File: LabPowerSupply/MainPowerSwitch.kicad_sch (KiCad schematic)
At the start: 3 parts

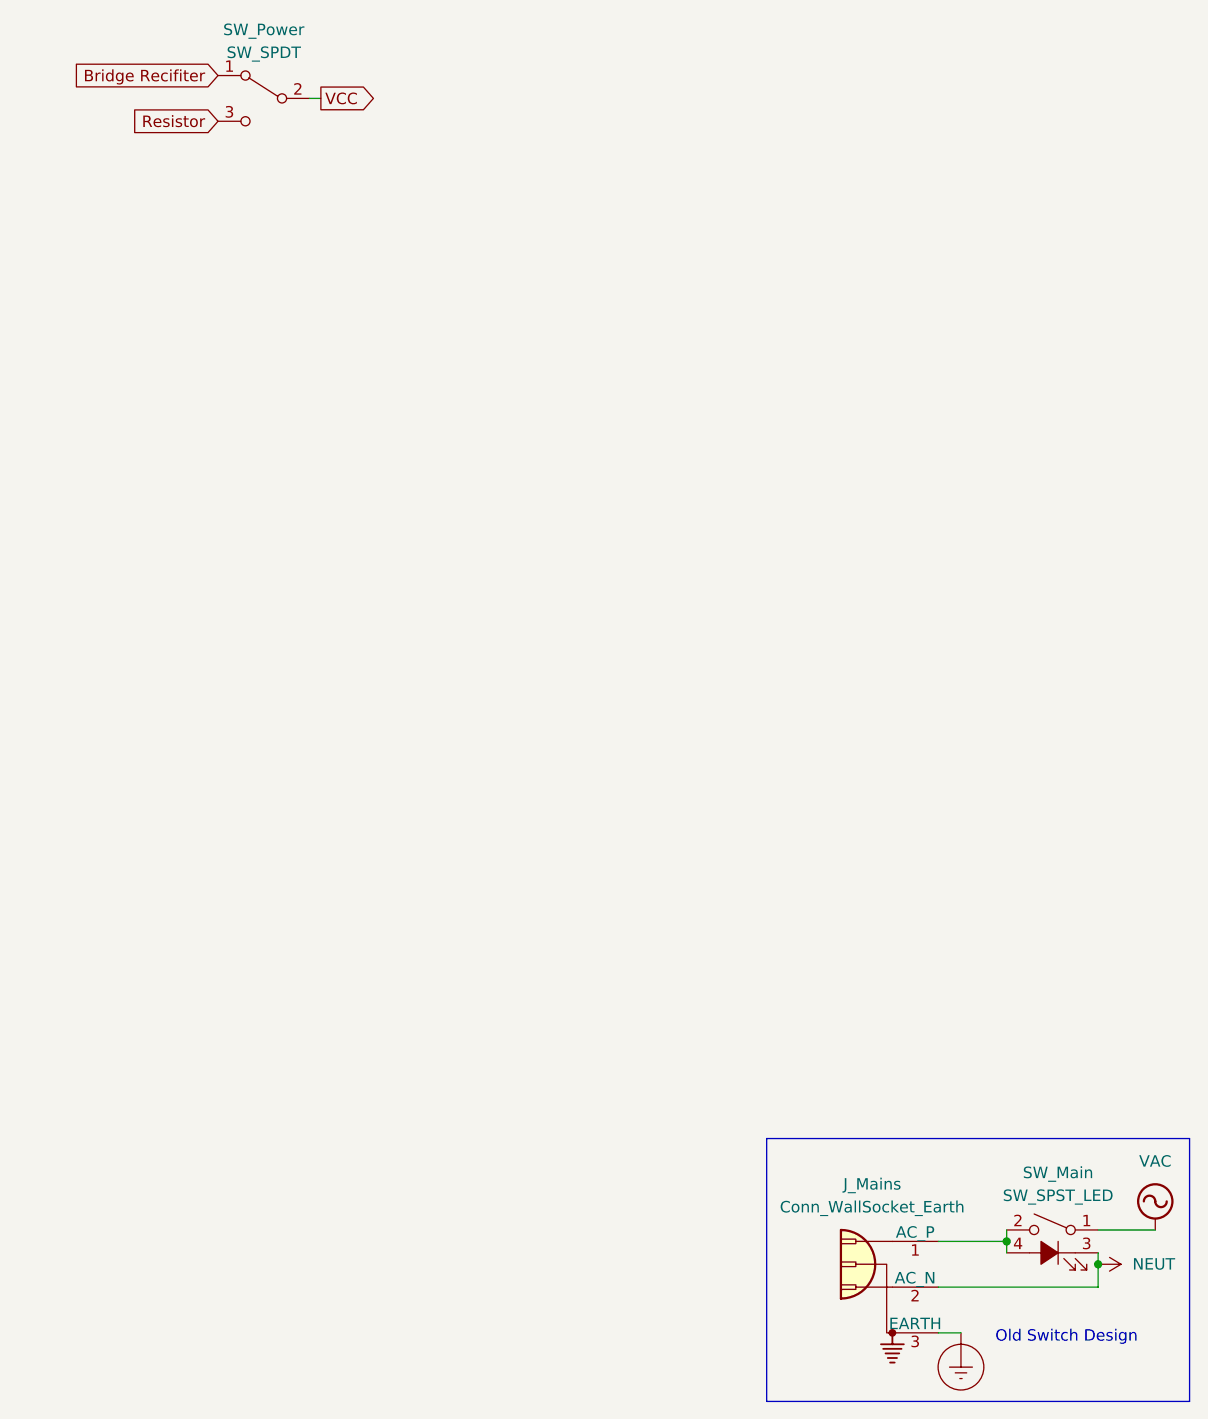
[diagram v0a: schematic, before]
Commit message: Finished first pass on the schematic
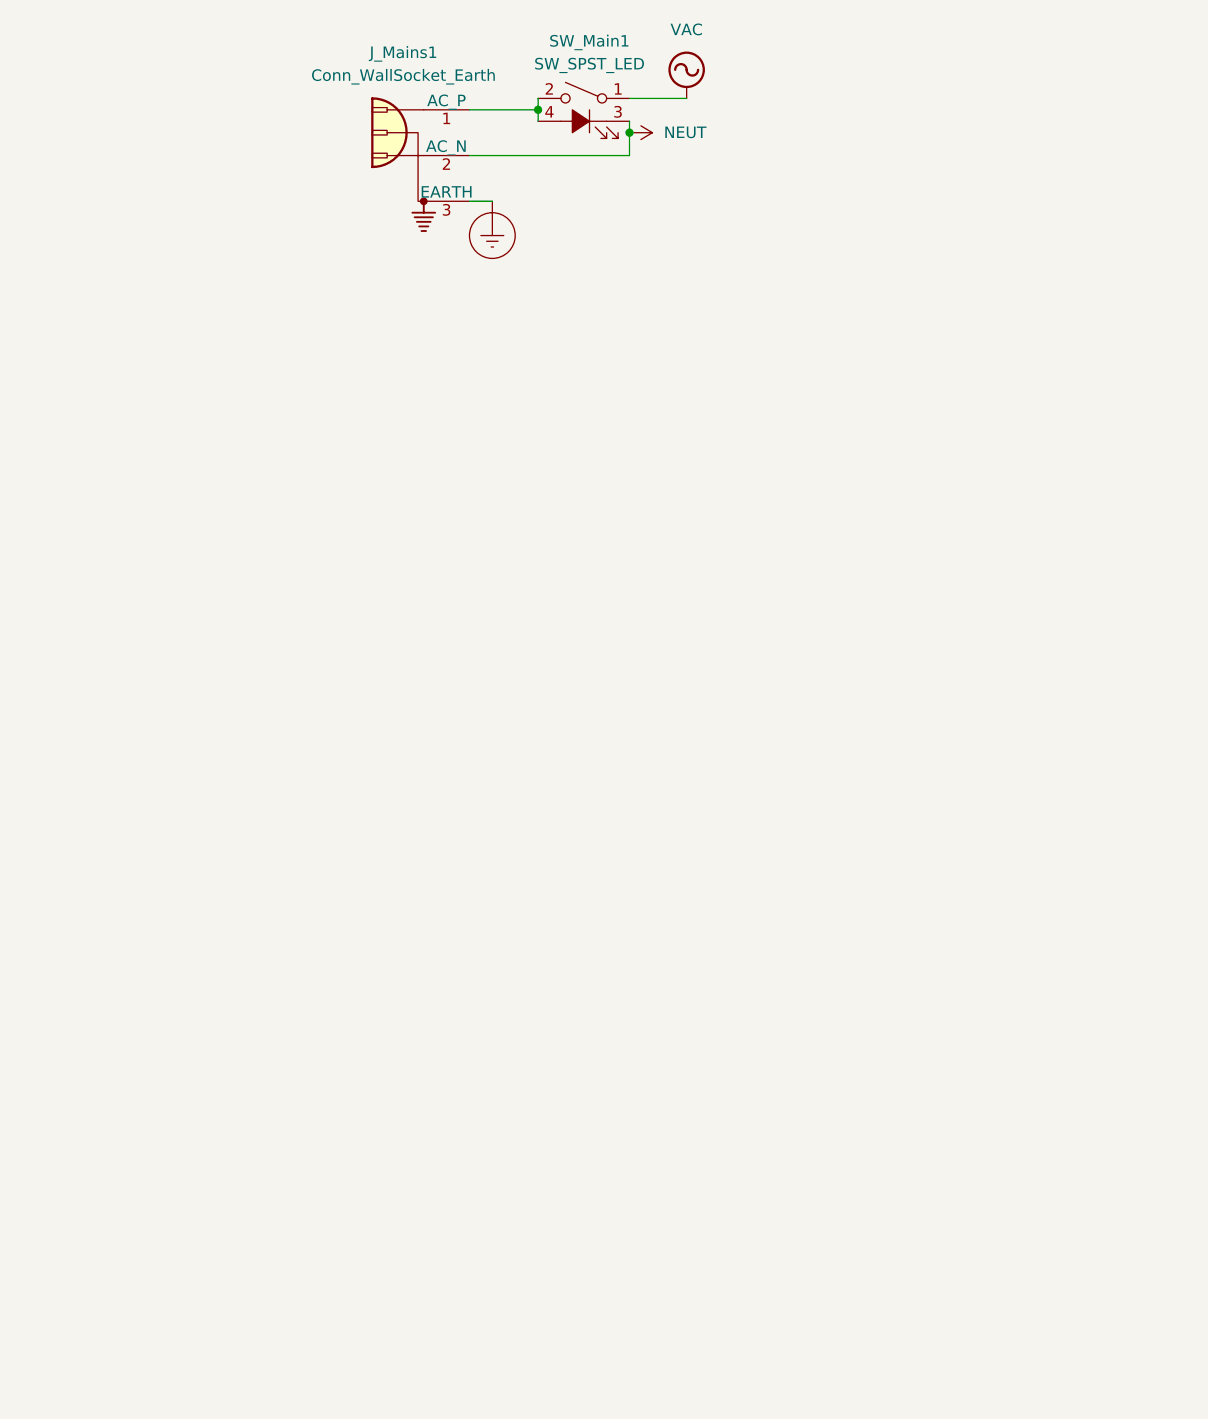
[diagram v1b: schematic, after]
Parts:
- removed SW_Power: SW_SPDT, symbol Switch:SW_SPDT
- renumbered J_Mains to J_Mains1, SW_Main to SW_Main1
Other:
- note removed: "Old Switch Design"
- moved on the sheet: J_Mains1, SW_Main1
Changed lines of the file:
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@@
     (title "Main Power Switch with Red LED")
     (date "2022-09-12")
-    (rev "1")
+    (rev "2")
     (company "George Mason University")
+    (comment 1 "ground the metal case.")
+    (comment 2 "of the transformer. There is also a built-in LED and earth wire to")
+    (comment 3 "The switch will connect the AC mains power to the primary side")
+    (comment 4 "This is just a model for how the main On/Off switch will work.")
   )
-  (junction (at 288.29 267.97) (diameter 0) (color 0 0 0 0)
+  (junction (at 236.22 142.24) (diameter 0) (color 0 0 0 0)
   )
-  (junction (at 278.13 265.43) (diameter 0) (color 0 0 0 0)
+  (junction (at 226.06 139.7) (diameter 0) (color 0 0 0 0)
   )
-  (wire (pts (xy 288.29 270.51) (xy 288.29 267.97))
+  (wire (pts (xy 236.22 144.78) (xy 236.22 142.24))
     (stroke (width 0) (type default) (color 0 0 0 0))
   )
-  (wire (pts (xy 288.29 264.16) (xy 294.64 264.16))
+  (wire (pts (xy 236.22 138.43) (xy 242.57 138.43))
     (stroke (width 0) (type default) (color 0 0 0 0))
   )
-  (polyline (pts (xy 251.46 254) (xy 298.45 254))
+  (wire (pts (xy 236.22 142.24) (xy 236.22 140.97))
     (stroke (width 0) (type default) (color 0 0 0 0))
   )
-  (wire (pts (xy 288.29 267.97) (xy 288.29 266.7))
+  (wire (pts (xy 218.44 144.78) (xy 236.22 144.78))
     (stroke (width 0) (type default) (color 0 0 0 0))
   )
-  (wire (pts (xy 270.51 270.51) (xy 288.29 270.51))
+  (wire (pts (xy 226.06 139.7) (xy 226.06 140.97))
     (stroke (width 0) (type default) (color 0 0 0 0))
   )
-  (polyline (pts (xy 298.45 283.21) (xy 251.46 283.21))
+  (wire (pts (xy 220.98 149.86) (xy 218.44 149.86))
     (stroke (width 0) (type default) (color 0 0 0 0))
   )
-  (wire (pts (xy 278.13 265.43) (xy 278.13 266.7))
+  (wire (pts (xy 218.44 139.7) (xy 226.06 139.7))
     (stroke (width 0) (type default) (color 0 0 0 0))
   )
-  (polyline (pts (xy 251.46 254) (xy 251.46 283.21))
+  (wire (pts (xy 226.06 138.43) (xy 226.06 139.7))
     (stroke (width 0) (type default) (color 0 0 0 0))
   )
-  (polyline (pts (xy 298.45 254) (xy 298.45 283.21))
-    (stroke (width 0) (type default) (color 0 0 0 0))
-  )
-  (wire (pts (xy 273.05 275.59) (xy 270.51 275.59))
-    (stroke (width 0) (type default) (color 0 0 0 0))
-  )
-  (wire (pts (xy 270.51 265.43) (xy 278.13 265.43))
-    (stroke (width 0) (type default) (color 0 0 0 0))
-  )
-  (wire (pts (xy 200.66 138.43) (xy 201.93 138.43))
-    (stroke (width 0) (type default) (color 0 0 0 0))
-  )
-  (wire (pts (xy 278.13 264.16) (xy 278.13 265.43))
-    (stroke (width 0) (type default) (color 0 0 0 0))
-  )
-  (text "Old Switch Design" (at 276.86 276.86 0)
-    (effects (font (size 1.27 1.27)) (justify left bottom))
-  )
-  (global_label "VCC" (shape output) (at 201.93 138.43 0) (fields_autoplaced)
-    (effects (font (size 1.27 1.27)) (justify left))
-    (property "Intersheet References" "${INTERSHEET_REFS}" (id 0) (at 207.9717 138.3506 0)
-      (effects (font (size 1.27 1.27)) (justify left) hide)
-    )
-  )
-  (global_label "Bridge Recifiter" (shape input) (at 190.5 135.89 180) (fields_autoplaced)
-    (effects (font (size 1.27 1.27)) (justify right))
-    (property "Intersheet References" "${INTERSHEET_REFS}" (id 0) (at 173.0888 135.8106 0)
-      (effects (font (size 1.27 1.27)) (justify right) hide)
-    )
-  )
-  (global_label "Resistor" (shape input) (at 190.5 140.97 180) (fields_autoplaced)
-    (effects (font (size 1.27 1.27)) (justify right))
-    (property "Intersheet References" "${INTERSHEET_REFS}" (id 0) (at 180.4064 140.8906 0)
-      (effects (font (size 1.27 1.27)) (justify right) hide)
-    )
-  )
-  (symbol (lib_id "Switch:SW_SPST_LED") (at 283.21 266.7 0) (mirror y) (unit 1)
+  (symbol (lib_id "Switch:SW_SPST_LED") (at 231.14 140.97 0) (mirror y) (unit 1)
     (in_bom yes) (on_board yes) (fields_autoplaced)
-    (property "Reference" "SW_Main" (id 0) (at 283.845 257.81 0))
-    (property "Value" "SW_SPST_LED" (id 1) (at 283.845 260.35 0))
-    (property "Footprint" "" (id 2) (at 283.21 259.08 0)
+    (property "Reference" "SW_Main1" (id 0) (at 231.775 132.08 0))
+    (property "Value" "SW_SPST_LED" (id 1) (at 231.775 134.62 0))
+    (property "Footprint" "" (id 2) (at 231.14 133.35 0)
       (effects (font (size 1.27 1.27)) hide)
     )
-    (property "Datasheet" "~" (id 3) (at 283.21 259.08 0)
+    (property "Datasheet" "~" (id 3) (at 231.14 133.35 0)
       (effects (font (size 1.27 1.27)) hide)
     )
@@
     (pin "4")
   )
-  (symbol (lib_id "power:VAC") (at 294.64 264.16 0) (unit 1)
+  (symbol (lib_id "power:VAC") (at 242.57 138.43 0) (unit 1)
     (in_bom yes) (on_board yes) (fields_autoplaced)
-    (property "Reference" "#PWR?" (id 0) (at 294.64 266.7 0)
+    (property "Reference" "#PWR03" (id 0) (at 242.57 140.97 0)
       (effects (font (size 1.27 1.27)) hide)
     )
-    (property "Value" "VAC" (id 1) (at 294.64 256.54 0))
-    (property "Footprint" "" (id 2) (at 294.64 264.16 0)
+    (property "Value" "VAC" (id 1) (at 242.57 130.81 0))
+    (property "Footprint" "" (id 2) (at 242.57 138.43 0)
       (effects (font (size 1.27 1.27)) hide)
     )
-    (property "Datasheet" "" (id 3) (at 294.64 264.16 0)
+    (property "Datasheet" "" (id 3) (at 242.57 138.43 0)
       (effects (font (size 1.27 1.27)) hide)
     )
     (pin "1")
   )
-  (symbol (lib_id "Switch:SW_SPDT") (at 195.58 138.43 0) (mirror y) (unit 1)
+  (symbol (lib_id "Connector:Conn_WallSocket_Earth") (at 213.36 144.78 0) (mirror y) (unit 1)
     (in_bom yes) (on_board yes) (fields_autoplaced)
-    (property "Reference" "SW_Power" (id 0) (at 195.58 130.81 0))
-    (property "Value" "SW_SPDT" (id 1) (at 195.58 133.35 0))
-    (property "Footprint" "" (id 2) (at 195.58 138.43 0)
+    (property "Reference" "J_Mains1" (id 0) (at 211.1248 133.35 0))
+    (property "Value" "Conn_WallSocket_Earth" (id 1) (at 211.1248 135.89 0))
+    (property "Footprint" "" (id 2) (at 220.98 142.24 0)
       (effects (font (size 1.27 1.27)) hide)
     )
-    (property "Datasheet" "~" (id 3) (at 195.58 138.43 0)
+    (property "Datasheet" "~" (id 3) (at 220.98 142.24 0)
       (effects (font (size 1.27 1.27)) hide)
     )
@@
     (pin "3")
   )
-  (symbol (lib_id "Connector:Conn_WallSocket_Earth") (at 265.43 270.51 0) (mirror y) (unit 1)
+  (symbol (lib_id "power:Earth_Protective") (at 220.98 149.86 0) (unit 1)
     (in_bom yes) (on_board yes) (fields_autoplaced)
-    (property "Reference" "J_Mains" (id 0) (at 263.1948 259.08 0))
-    (property "Value" "Conn_WallSocket_Earth" (id 1) (at 263.1948 261.62 0))
-    (property "Footprint" "" (id 2) (at 273.05 267.97 0)
+    (property "Reference" "#PWR01" (id 0) (at 227.33 156.21 0)
       (effects (font (size 1.27 1.27)) hide)
     )
-    (property "Datasheet" "~" (id 3) (at 273.05 267.97 0)
+    (property "Value" "Earth_Protective" (id 1) (at 232.41 153.67 0)
       (effects (font (size 1.27 1.27)) hide)
     )
-    (pin "1")
-    (pin "2")
-    (pin "3")
-  )
-  (symbol (lib_id "power:Earth_Protective") (at 273.05 275.59 0) (unit 1)
-    (in_bom yes) (on_board yes) (fields_autoplaced)
-    (property "Reference" "#PWR?" (id 0) (at 279.4 281.94 0)
+    (property "Footprint" "" (id 2) (at 220.98 152.4 0)
       (effects (font (size 1.27 1.27)) hide)
     )
-    (property "Value" "Earth_Protective" (id 1) (at 284.48 279.4 0)
-      (effects (font (size 1.27 1.27)) hide)
-    )
-    (property "Footprint" "" (id 2) (at 273.05 278.13 0)
-      (effects (font (size 1.27 1.27)) hide)
-    )
-    (property "Datasheet" "~" (id 3) (at 273.05 278.13 0)
+    (property "Datasheet" "~" (id 3) (at 220.98 152.4 0)
       (effects (font (size 1.27 1.27)) hide)
     )
     (pin "1")
   )
-  (symbol (lib_id "power:NEUT") (at 288.29 267.97 270) (unit 1)
+  (symbol (lib_id "power:NEUT") (at 236.22 142.24 270) (unit 1)
     (in_bom yes) (on_board yes) (fields_autoplaced)
-    (property "Reference" "#PWR?" (id 0) (at 284.48 267.97 0)
+    (property "Reference" "#PWR02" (id 0) (at 232.41 142.24 0)
       (effects (font (size 1.27 1.27)) hide)
     )
-    (property "Value" "NEUT" (id 1) (at 292.1 267.9699 90)
+    (property "Value" "NEUT" (id 1) (at 240.03 142.2399 90)
       (effects (font (size 1.27 1.27)) (justify left))
     )
-    (property "Footprint" "" (id 2) (at 288.29 267.97 0)
+    (property "Footprint" "" (id 2) (at 236.22 142.24 0)
       (effects (font (size 1.27 1.27)) hide)
     )
-    (property "Datasheet" "" (id 3) (at 288.29 267.97 0)
+    (property "Datasheet" "" (id 3) (at 236.22 142.24 0)
       (effects (font (size 1.27 1.27)) hide)
     )
